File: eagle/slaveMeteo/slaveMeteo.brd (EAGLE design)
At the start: 14 x 21.6 mm, 35 parts, among them J1 RJ12RIGHTANGLE-I2C, Q1 CMA-4544PF-W, U2 MAX4466EXK+T, X1 1503_09

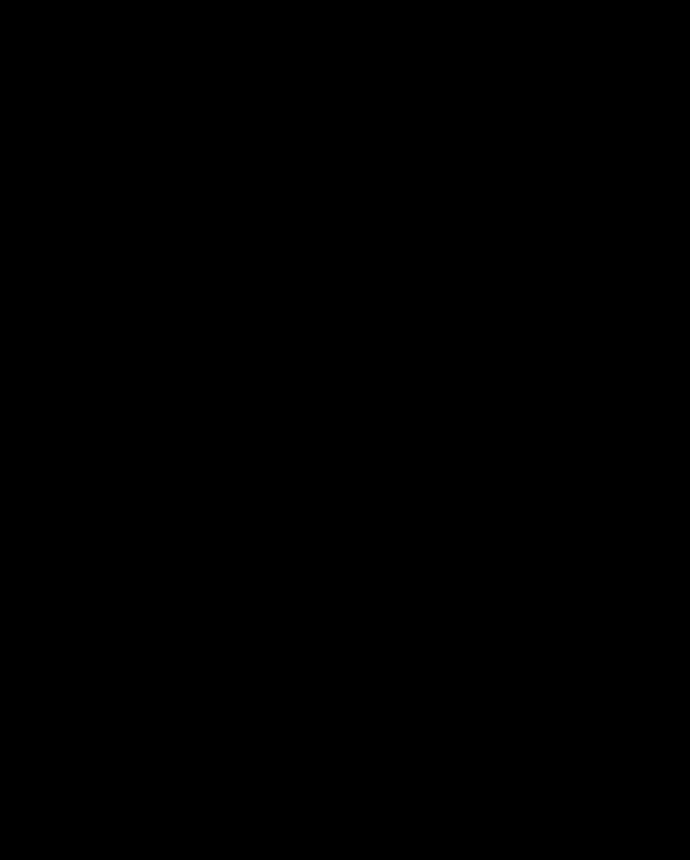
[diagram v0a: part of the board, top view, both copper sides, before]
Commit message: updated eagle libraries and readme, started designing meteo station
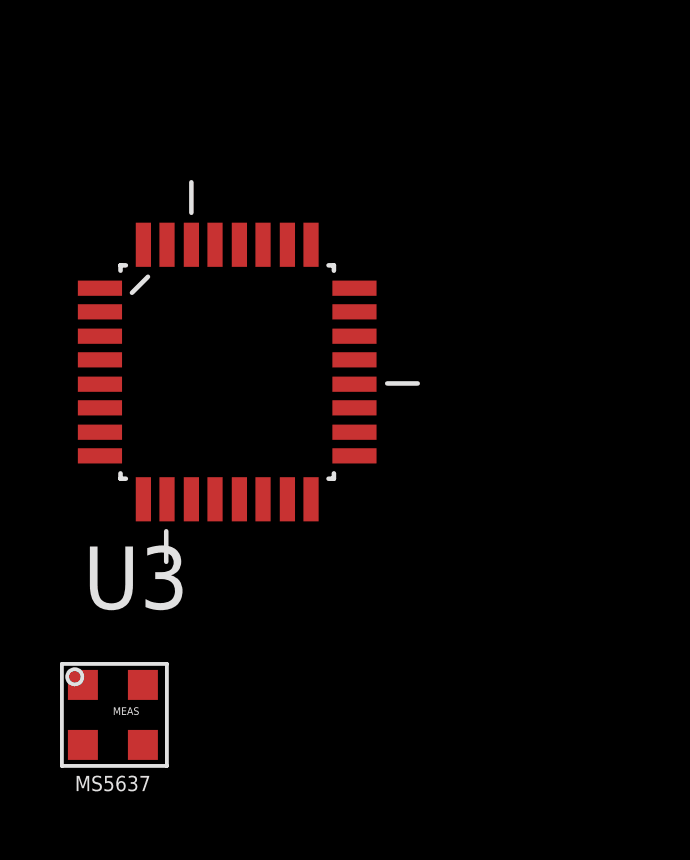
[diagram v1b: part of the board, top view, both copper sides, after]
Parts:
- added U$19: MS5637, MS5637:MS5637
- added U3: ATMEGA328P-AU, Ava:QFP80P900X900X120-32N
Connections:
- new net VCC_2: U3.4
- net AVCC: now also U3.18
- net VCC: now also U3.6
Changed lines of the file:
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@@
 <?xml version="1.0" encoding="utf-8"?>
 <!DOCTYPE eagle SYSTEM "eagle.dtd">
-<eagle version="8.2.2">
+<eagle version="9.0.0">
 <drawing>
 <settings>
 <setting alwaysvectorfont="no"/>
+<setting keepoldvectorfont="yes"/>
 <setting verticaltext="up"/>
 </settings>
@@
 <param name="dpMaxLengthDifference" value="10mm"/>
 <param name="dpGapFactor" value="2.5"/>
-<param name="checkGrid" value="0"/>
 <param name="checkAngle" value="0"/>
 <param name="checkFont" value="1"/>
 <param name="checkRestrict" value="1"/>
+<param name="checkStop" value="0"/>
+<param name="checkValues" value="0"/>
 <param name="useDiameter" value="13"/>
 <param name="maxErrors" value="50"/>
@@
 <element name="U$17" library="microbuilder" package="ADAFRUIT_2.5MM" value="" x="-35.306" y="-190.119"/>
 <element name="U$18" library="microbuilder" package="ADAFRUIT_2.5MM" value="" x="-32.512" y="-189.23" rot="MR0"/>
+<element name="U3" library="Ava" package="QFP80P900X900X120-32N" value="ATMEGA328P-AU" x="-63.5" y="-207.01">
+<attribute name="DESCRIPTION" value="8-bit Microcontroller with In-System Programmable Flash" x="-63.5" y="-207.01" size="1.778" layer="27" display="off"/>
+<attribute name="MPN" value="ATMEGA328P-AU" x="-63.5" y="-207.01" size="1.778" layer="27" display="off"/>
+<attribute name="OC_FARNELL" value="1715486" x="-63.5" y="-207.01" size="1.778" layer="27" display="off"/>
+<attribute name="OC_NEWARK" value="14R4631" x="-63.5" y="-207.01" size="1.778" layer="27" display="off"/>
+<attribute name="PACKAGE" value="TQFP-32" x="-63.5" y="-207.01" size="1.778" layer="27" display="off"/>
+<attribute name="SUPPLIER" value="Atmel" x="-63.5" y="-207.01" size="1.778" layer="27" display="off"/>
+</element>
+<element name="U$19" library="MS5637" package="MS5637" value="MS5637" x="-67.31" y="-218.44"/>
 </elements>
 <signals>
@@
 <wire x1="-37.211" y1="-206.756" x2="-39.116" y2="-204.851" width="0.4064" layer="1"/>
 <wire x1="-39.116" y1="-204.851" x2="-39.116" y2="-203.515" width="0.4064" layer="1"/>
+<contactref element="U3" pad="6"/>
+<wire x1="-67.7418" y1="-208.2038" x2="-39.116" y2="-204.851" width="0" layer="19" extent="1-1"/>
 </signal>
 <signal name="N$2">
@@
 <wire x1="-39.116" y1="-201.615" x2="-39.243" y2="-201.869" width="0.4064" layer="1"/>
 <wire x1="-39.243" y1="-201.869" x2="-39.243" y2="-200.152" width="0.4064" layer="1"/>
+<contactref element="U3" pad="18"/>
+<wire x1="-59.2582" y1="-209.0166" x2="-39.243" y2="-201.869" width="0" layer="19" extent="1-1"/>
 </signal>
 <signal name="AGND">
@@
 <wire x1="-35.002" y1="-203.819" x2="-33.169" y2="-203.819" width="0.4064" layer="1"/>
 </signal>
+<signal name="VCC_2">
+<contactref element="U3" pad="4"/>
+</signal>
 </signals>
 </board>
@@
 <compatibility>
 <note version="8.2" severity="warning">
-Since Version 8.2, Eagle supports online libraries. The ids
+Since Version 8.2, EAGLE supports online libraries. The ids
 of those online libraries will not be understood (or retained)
 with this version.

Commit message: connected components on Slave meteo. Kept backup in case we still need a sound detector
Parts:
- removed C5: 10uF, microbuilder:0805
- removed FB1, FB2: FERRITE, microbuilder:0805
- removed FID1, FID2: FIDUCIAL"", microbuilder:FIDUCIAL_1MM
- removed JP1: (no value), microbuilder:1X03_ROUND_76
- removed Q1: CMA-4544PF-W, microbuilder:ELECTRET_9.7
- removed R10, R11: 1K, microbuilder:0805
- removed R12, R13: 1M, microbuilder:0805
- removed R14: 22K, microbuilder:0805
- removed U$14, U$15: MOUNTINGHOLE2.5, microbuilder:MOUNTINGHOLE_2.5_PLATED
- removed U$17, U$18: (no value), microbuilder:ADAFRUIT_2.5MM
- removed U2: MAX4466EXK+T, microbuilder:SC70-5
- removed VR1: TC33X-2-104E (100K), microbuilder:TRIMPOT_BOURNS_TC33X-2
- added S1: Reset, Testing:TACTILE-SWITCH-SMD-ALT01
- C2: value 0.1µF -> 100nF; device microbuilder:0805 -> rcl:C0805K
- C3: value 0.01uF -> 100nF; device microbuilder:0805 -> rcl:C0805K
- C4: value 100pF -> 100nF; device microbuilder:0805 -> rcl:C0805K
- R9: value 1K -> 10k; device microbuilder:0805 -> rcl:R0805
- U3: value ATMEGA328P-AU -> ATMEGA328; device Ava:QFP80P900X900X120-32N -> SparkFun:TQFP32-08
- moved U$19 289.7 mm to (78.7, 31.8)
- moved U3 264.0 mm to (40.6, 35.6)
- moved R9 250.5 mm to (71.1, 33.0)
- moved C4 228.0 mm to (43.2, 14.0), turned to 0 degrees
- moved C3 221.3 mm to (36.8, 14.0), turned to 0 degrees
- moved C2 220.3 mm to (30.5, 14.0), turned to 0 degrees
- moved R4 201.0 mm to (2.54, 33.0)
- moved R5 201.0 mm to (2.54, 26.7)
- moved C1 201.0 mm to (2.54, 39.4)
- moved R7 201.0 mm to (2.54, 20.3)
- moved R8 201.0 mm to (2.54, 14.0)
- moved R6 177.4 mm to (83.8, 16.5)
- moved X1 174.9 mm to (61.0, 15.2)
- moved R2 173.1 mm to (54.9, 64.8)
- moved R3 167.5 mm to (19.1, 52.1)
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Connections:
- removed net AGND: C2.2, C5.2, FB1.2, Q1.-, R12.1, U2.2
- removed net AVCC: FB2.1, R10.2, R13.2, U2.5, U3.18
- removed net N$1: R1.2, R2.1
- removed net N$10: C5.1, R11.1
- removed net N$11: R14.2, VR1.3
- removed net N$2: C3.1, Q1.+, R9.1
- removed net N$3: R3.1, U$1.DQ
- removed net N$6: C2.1, R10.1, R9.2
- removed net N$7: C3.2, R12.2, R13.1, U2.1
- removed net N$8: C4.1, JP1.3, U2.4, VR1.1, VR1.2
- removed net N$9: C4.2, R11.2, R14.1, U2.3
- removed net VCC_2: U3.4
- new net 3.3V: J1.+5V
- new net A0: R3.1, U$1.DQ, U3.23
- new net A1: R1.2, R2.1, U3.24
- new net A2: U1.DATA, U3.25
- new net A3: U3.26
- new net A7: U3.22
- new net AREF: C3.1, U3.20
- new net D10: U3.14
- new net D2: U3.32
- new net D3: U3.1
- new net D4: U3.2
- new net D5: U3.9
- new net D6: U3.10
- new net D7: U3.11
- new net D8: U3.12
- new net D9: U3.13
- new net DTR: C2.1
- new net MISO: U3.16
- new net MOSI: U3.15
- new net RESET: C2.2, R9.1, S1.3, S1.4, U3.29
- new net RX: U3.30
- new net SCK: U3.17
- new net TX: U3.31
- net +5V: no longer J1.+5V
- net A6: now also U3.19
- net GND: now also C3.2, C4.2, S1.1, S1.2, U$19.GND, U3.21, U3.3, U3.5; no longer FB1.1, JP1.2
- net SCL: now also U$19.SCL, U3.28
- net SDA: now also U$19.SDA, U3.27
- net VCC: now also C4.1, R9.2, U$19.VDD, U3.18, U3.4; no longer FB2.2, JP1.1
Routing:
- net AVCC: track 24.3 -> 0.00 mm, vias 2 -> 0
- net N$8: track 12.4 -> 0.00 mm
- net AGND: track 11.8 -> 0.00 mm, vias 3 -> 0
- net N$9: track 10.2 -> 0.00 mm
- net N$7: track 9.23 -> 0.00 mm
- net GND: track 5.46 -> 0.00 mm
- net N$6: track 5.44 -> 0.00 mm
- net N$2: track 5.36 -> 0.00 mm
- net VCC: track 5.17 -> 0.00 mm
- net N$10: track 2.16 -> 0.00 mm
- net N$11: track 2.14 -> 0.00 mm
- removed copper zone on layer 16, net AGND
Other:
- board size 14 x 21.6 mm -> 10.4 x 11.8 mm
- board text removed: "Adjustable gain"
- board text removed: "GND"
- board text removed: "MAX4466"
- board text removed: "MIC AMP"
- board text removed: "OUT"
- board text removed: "VCC"
- board text removed: "VCC: 2.4-5.5V"

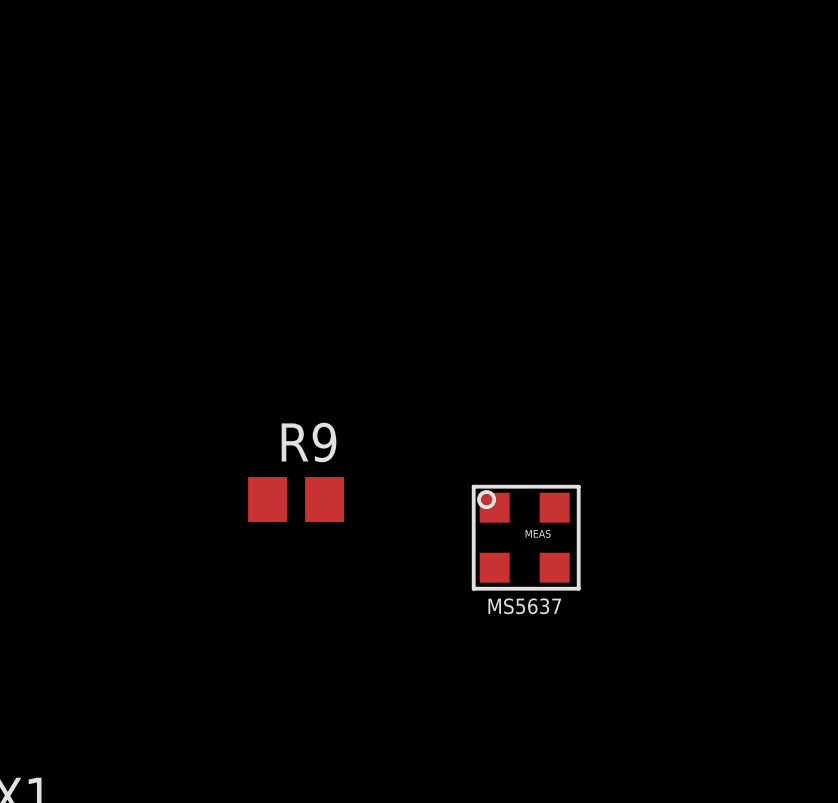
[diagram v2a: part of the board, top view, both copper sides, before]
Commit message: reorganized components oon brd file for meteoslave
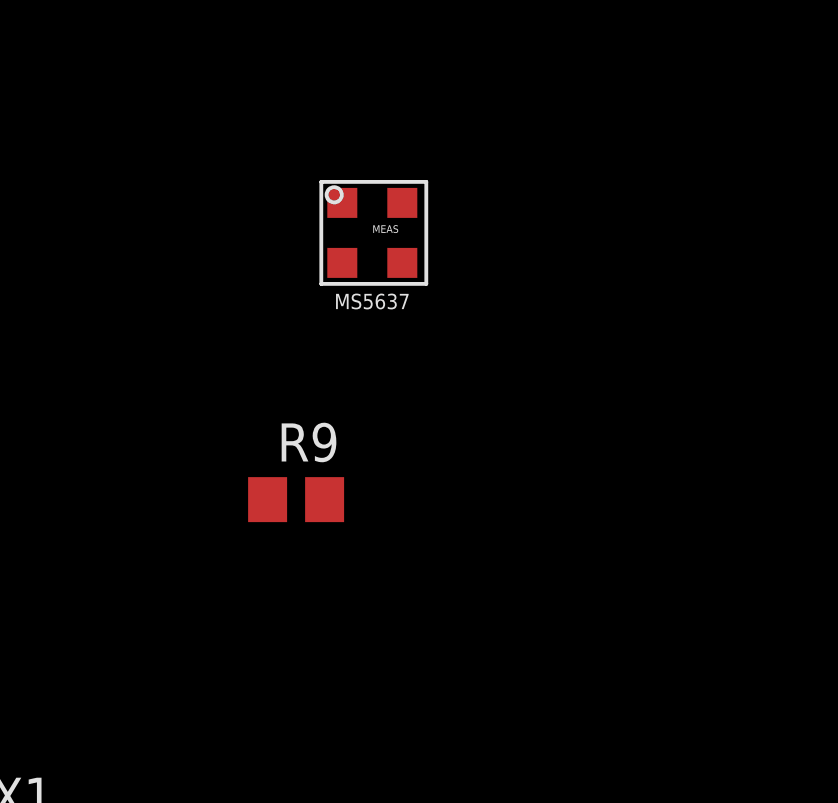
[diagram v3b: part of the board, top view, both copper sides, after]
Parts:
- moved U$19 11.4 mm to (73.7, 41.9)
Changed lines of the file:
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@@
 <element name="R7" library="resistor" library_urn="urn:adsk.eagle:library:348" package="R0805" value="" x="2.54" y="20.32"/>
 <element name="R8" library="resistor" library_urn="urn:adsk.eagle:library:348" package="R0805" value="100k" x="2.54" y="13.97"/>
-<element name="U$19" library="MS5637" package="MS5637" value="MS5637" x="78.74" y="31.75"/>
+<element name="U$19" library="MS5637" package="MS5637" value="MS5637" x="73.66" y="41.91"/>
 <element name="U3" library="SparkFun" package="TQFP32-08" value="ATMEGA328" x="40.64" y="35.56"/>
 <element name="S1" library="Testing" package="TACTILE-SWITCH-SMD-ALT01" value="Reset" x="34.29" y="7.62"/>
@@
 <wire x1="31.496" y1="9.525" x2="37.084" y2="9.525" width="0" layer="19" extent="1-1"/>
 <wire x1="44.18" y1="13.97" x2="37.83" y2="13.97" width="0" layer="19" extent="1-1"/>
-<wire x1="79.74" y1="32.75" x2="44.9326" y2="35.96" width="0" layer="19" extent="1-1"/>
+<wire x1="74.66" y1="42.91" x2="44.9326" y2="35.96" width="0" layer="19" extent="1-1"/>
 </signal>
 <signal name="SDA">
@@
 <contactref element="U3" pad="27"/>
 <contactref element="U$19" pad="SDA"/>
-<wire x1="41.84" y1="39.8526" x2="77.74" y2="30.75" width="0" layer="19" extent="1-1"/>
+<wire x1="41.84" y1="39.8526" x2="72.66" y2="40.91" width="0" layer="19" extent="1-1"/>
 <wire x1="25.9" y1="79.77" x2="41.84" y2="39.8526" width="0" layer="19" extent="1-1"/>
 </signal>
@@
 <contactref element="U3" pad="28"/>
 <contactref element="U$19" pad="SCL"/>
-<wire x1="41.04" y1="39.8526" x2="79.74" y2="30.75" width="0" layer="19" extent="1-1"/>
+<wire x1="41.04" y1="39.8526" x2="74.66" y2="40.91" width="0" layer="19" extent="1-1"/>
 <wire x1="26.94" y1="77.23" x2="41.04" y2="39.8526" width="0" layer="19" extent="1-1"/>
 </signal>
@@
 <contactref element="C4" pad="1"/>
 <contactref element="U$19" pad="VDD"/>
-<wire x1="72.07" y1="33.02" x2="77.74" y2="32.75" width="0" layer="19" extent="1-1"/>
+<wire x1="72.07" y1="33.02" x2="72.66" y2="42.91" width="0" layer="19" extent="1-1"/>
 <wire x1="44.9326" y1="33.56" x2="72.07" y2="33.02" width="0" layer="19" extent="1-1"/>
 <wire x1="42.18" y1="13.97" x2="44.9326" y2="33.56" width="0" layer="19" extent="1-1"/>

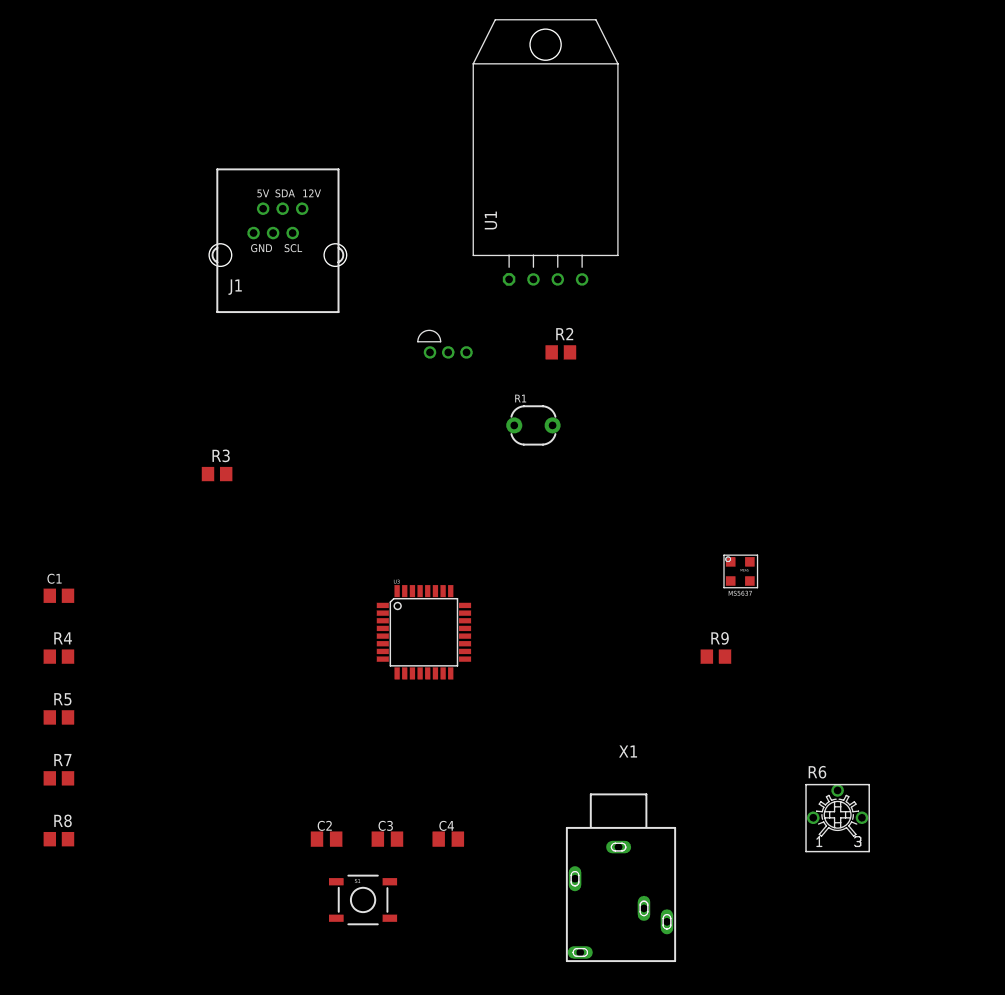
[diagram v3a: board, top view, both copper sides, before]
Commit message: redesigned meteoSlave using slave-basic
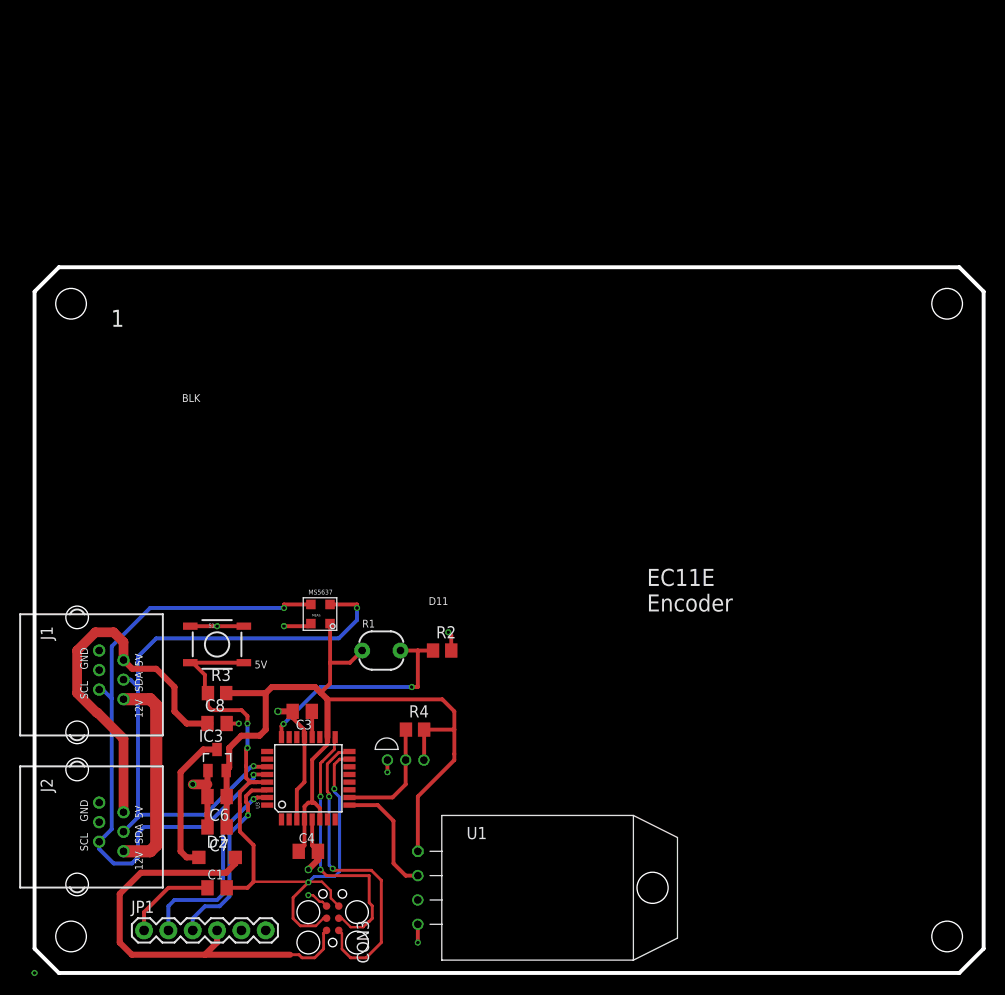
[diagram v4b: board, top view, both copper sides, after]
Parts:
- removed C2: 100nF, rcl:C0805K
- removed R5, R7: (no value), resistor:R0805
- removed R6: 10k, dp_devices:TRIMMER_3362P
- removed R8: 100k, resistor:R0805
- removed R9: 10k, rcl:R0805
- removed X1: 1503_09, con-lumberg:1503_09
- added C6, C8: 10u, rcl:C0805K
- added C7: 100nF, rcl:C0805K
- added CON3: SPI, lpatiny:TC2030-MCP
- added D2: Schottky, diode:SOD123
- added IC3: MCP1703CB, linear:SOT23
- added J2: RJ12RIGHTANGLE-I2C, lpatiny:RJ12-RIGHTANGLE-I2C
- added JP1: FTDI Basic, SparkFun:1X06
- C1: device dp_devices:C805 -> rcl:C0805K
- R3: value (none) -> 10k; device resistor:R0805 -> rcl:R0805
- R4: value 100k -> (none)
- moved U1 64.9 mm to (40.0, 8.89), turned to 270 degrees
- moved J1 48.6 mm to (4.45, 31.1), turned to 270 degrees
- moved U$19 44.0 mm to (29.8, 37.5), turned to 180 degrees
- moved U$1 42.8 mm to (36.2, 23.5)
- moved R4 37.9 mm to (39.7, 25.4)
- moved C1 34.7 mm to (19.1, 8.89)
- moved R2 33.5 mm to (42.5, 33.7)
- moved S1 30.7 mm to (19.1, 34.3)
- moved R1 28.4 mm to (36.2, 33.7)
- moved R3 22.9 mm to (19.1, 29.2)
- moved U3 19.4 mm to (28.6, 20.3), turned to 90 degrees
- moved C3 16.0 mm to (27.9, 27.3), turned to 180 degrees
- moved C4 14.7 mm to (28.6, 12.7)
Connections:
- removed net 3.3V: J1.+5V
- removed net GND1: R6.1
- removed net GND2: R8.1, X1.3
- removed net N$14: C1.2, X1.1
- removed net N$21: X1.2
- removed net N$4: J1.+12V
- removed net N$5: C1.1, R4.1, R8.2
- new net +12V: J1.+12V, J2.+12V
- new net EXT-VCC: CON3.5V, D2.A, JP1.4
- net +5V: now also C8.1, D2.C, IC3.3, J1.+5V, J2.+5V; no longer R1.1, R3.2, R4.2, U$1.VDD, U1.VDD
- net A0: no longer R3.1, U$1.DQ
- net A2: no longer U1.DATA
- net A6: no longer J1.GND2
- net D5: now also U1.DATA
- net D6: now also R4.1, U$1.DQ
- net DTR: now also C1.1, JP1.1; no longer C2.1
- net GND: now also C6.2, C7.2, C8.2, CON3.GND, IC3.1, J1.GND2, J2.GND1, J2.GND2, JP1.5, JP1.6
- net MISO: now also CON3.MISO
- net MOSI: now also CON3.MOSI
- net RESET: now also C1.2, CON3.RESET, R3.1; no longer C2.2, R9.1
- net RX: now also JP1.3
- net SCK: now also CON3.SCK
- net SCL: now also J2.SCL
- net SDA: now also J2.SDA
- net TX: now also JP1.2
- net VCC: now also C6.1, C7.1, IC3.2, R1.1, R3.2, R4.2, U$1.VDD, U1.VDD; no longer R9.2
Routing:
- net VCC: track 0.00 -> 95.6 mm
- net SCL: track 0.00 -> 69.9 mm, vias 0 -> 3
- net SDA: track 0.00 -> 65.5 mm, vias 0 -> 2
- net +5V: track 0.00 -> 55.2 mm
- net RESET: track 0.00 -> 49.5 mm, vias 0 -> 2
- net EXT-VCC: track 0.00 -> 46.5 mm
- net GND: track 0.00 -> 44.4 mm, vias 0 -> 10
- net MISO: track 0.00 -> 33.3 mm, vias 0 -> 2
- net SCK: track 0.00 -> 28.7 mm, vias 0 -> 2
- net MOSI: track 0.00 -> 25.5 mm, vias 0 -> 2
- net A1: track 0.00 -> 24.3 mm, vias 0 -> 2
- net +12V: track 0.00 -> 22.0 mm
- net TX: track 0.00 -> 21.5 mm, vias 0 -> 1
- net RX: track 0.00 -> 19.9 mm, vias 0 -> 1
- net D5: track 0.00 -> 12.8 mm
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- added copper zone on layer 16, net GND
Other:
- board size 10.4 x 11.8 mm -> 99.1 x 73.7 mm
- board text added: "1"
- board text added: "5V"
- board text added: "BLK"
- board text added: "Bio4_LCD_v1.1"
- board text added: "D11"
- board text added: "EC11E Encoder"
- board text added: "Simple spectro V 1.6.0"
- board text added: "Simple spectro V1.6.0"
